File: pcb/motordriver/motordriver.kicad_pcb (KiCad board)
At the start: 2 copper layers, 15 parts, among them J1 Conn_01x03_Pin, J2 Conn_01x02_Pin, J3 Conn_01x02_Pin, J4 Conn_01x03_Pin, U1 ESP32-CAM, U2 DRV8833PWP

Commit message: PCB created
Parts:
- removed U1: ESP32-CAM, _for_motordriver:ESP32-CAM
- added C5: 22uF, Capacitor_SMD:C_1206_3216Metric, F.Cu at (103.5, 120.4)
- added C6: 22uF, Capacitor_SMD:C_1206_3216Metric, F.Cu at (145.1, 119.8)
- added H1: ~, PCM_JLCPCB:Hole_Tooling_JLCPCB, F.Cu at (101.5, 101.5)
- added H2: ~, PCM_JLCPCB:Hole_Tooling_JLCPCB, F.Cu at (101.5, 123.5)
- added H3: ~, PCM_JLCPCB:Hole_Tooling_JLCPCB, F.Cu at (147.5, 101.5)
- added J5: Conn_02x03_Odd_Even, Connector_PinHeader_2.54mm:PinHeader_2x03_P2.54mm_Horizontal, F.Cu at (141.6, 116.6)
- added R6: 5k1, Resistor_SMD:R_0603_1608Metric, F.Cu at (116.0, 104.2)
- added R7: 5k1, Resistor_SMD:R_0603_1608Metric, F.Cu at (117.8, 103.5)
- C3: renamed from C2; value 10uF -> 22uF; footprint Capacitor_SMD:C_1210_3225Metric -> Capacitor_SMD:C_1206_3216Metric
- C4: value 10uF -> 22uF; footprint Capacitor_SMD:C_1210_3225Metric -> Capacitor_SMD:C_1206_3216Metric
- J1: value Conn_01x03_Pin -> USB_C_Receptacle_PowerOnly_6P; footprint Connector_PinHeader_2.54mm:PinHeader_1x03_P2.54mm_Horizontal -> Connector_USB:USB_C_Receptacle_HRO_TYPE-C-31-M-17
- J2, J3: value Conn_01x02_Pin -> Conn_01x08_Pin; footprint Connector_PinHeader_2.54mm:PinHeader_1x02_P2.54mm_Vertical -> Connector_PinSocket_2.54mm:PinSocket_1x08_P2.54mm_Vertical
- J4: value Conn_01x03_Pin -> Conn_02x03_Odd_Even; footprint Connector_PinHeader_2.54mm:PinHeader_1x03_P2.54mm_Horizontal -> Connector_PinHeader_2.54mm:PinHeader_2x03_P2.54mm_Horizontal
- moved U2 62.2 mm to (124.1, 116.0)
- moved J2 60.8 mm to (136.0, 119.8), turned to 180 degrees
- moved C4 56.0 mm to (131.6, 120.4)
- moved R5 55.7 mm to (108.3, 120.4)
- moved R4 54.9 mm to (140.2, 119.8)
- moved R3 54.0 mm to (116.3, 118.4), turned to 90 degrees
- moved R1 53.7 mm to (120.0, 110.5), turned to 180 degrees
- moved C1 52.8 mm to (129.4, 113.6), turned to -90 degrees
- moved C3 52.5 mm to (124.9, 110.5)
- moved C2 52.5 mm to (129.2, 116.9), turned to -90 degrees
- moved R2 52.5 mm to (116.3, 113.6), turned to -90 degrees
- moved J4 49.6 mm to (102.5, 116.6), turned to 90 degrees
- moved J3 47.7 mm to (113.0, 102.0)
- moved J1 45.5 mm to (124.5, 104.0), turned to 180 degrees
- renumbered C3 to C2
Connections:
- J2 pad 1: Net-(J2-Pin_1) -> +5V
- J2 pad 2: Net-(J2-Pin_2) -> GND
- J3 pad 1: Net-(J3-Pin_1) -> GND
- J3 pad 2: Net-(J3-Pin_2) -> unconnected-(J3-Pin_2-Pad2)
- J4 pad 1: GND -> unconnected-(J4-Pin_1-Pad1)
- J4 pad 2: Net-(J4-Pin_2) -> /Servo2
- J4 pad 3: /Servo2 -> Net-(J4-Pin_3)
- R4 pad 2: Net-(J1-Pin_2) -> Net-(J5-Pin_4)
- R5 pad 1: +5V -> Net-(J4-Pin_4)
- R5 pad 2: Net-(J4-Pin_2) -> +5V
- U2 pad 2: Net-(J2-Pin_2) -> Net-(J4-Pin_3)
- U2 pad 4: Net-(J2-Pin_1) -> Net-(J4-Pin_5)
- U2 pad 5: Net-(J3-Pin_1) -> Net-(J5-Pin_5)
- U2 pad 7: Net-(J3-Pin_2) -> Net-(J5-Pin_3)
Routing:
- net +5V: track 0.00 -> 59.5 mm, vias 0 -> 4
- net Net-(J5-Pin_5): track 0.00 -> 43.2 mm, vias 0 -> 2
- net Net-(J5-Pin_3): track 0.00 -> 35.5 mm
- net Net-(U2-VM): track 0.00 -> 22.7 mm, vias 0 -> 2
- net /MotorL2: track 0.00 -> 20.6 mm
- net GND: track 0.00 -> 20.6 mm, vias 0 -> 16
- net /MotorL1: track 0.00 -> 19.0 mm, vias 0 -> 1
- net Net-(J4-Pin_3): track 0.00 -> 17.9 mm
- net Net-(J4-Pin_5): track 0.00 -> 14.1 mm
- net /Servo2: track 0.00 -> 13.5 mm
- net /Servo1: track 0.00 -> 12.6 mm
- net /MotorR1: track 0.00 -> 11.9 mm, vias 0 -> 2
- net /MotorR2: track 0.00 -> 10.1 mm
- net Net-(J1-CC2): track 0.00 -> 9.53 mm
- net Net-(J4-Pin_4): track 0.00 -> 9.22 mm
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- added copper zone on B.Cu, net +5V
- added copper zone on B.Cu, net GND
- added copper zone on F.Cu, net GND
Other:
- board outline added: 49 x 25 mm
- board text added: "JLCJLCJLCJLC"
- board text added: "Motor driver for ESP-CAM, LL2026 Hackerspace FFM e.V. https://github.com/hackffm/ESP32_CAM_Auto"
- board text added: "MotorLeft Servo1"
- board text added: "MotorRight Servo2"

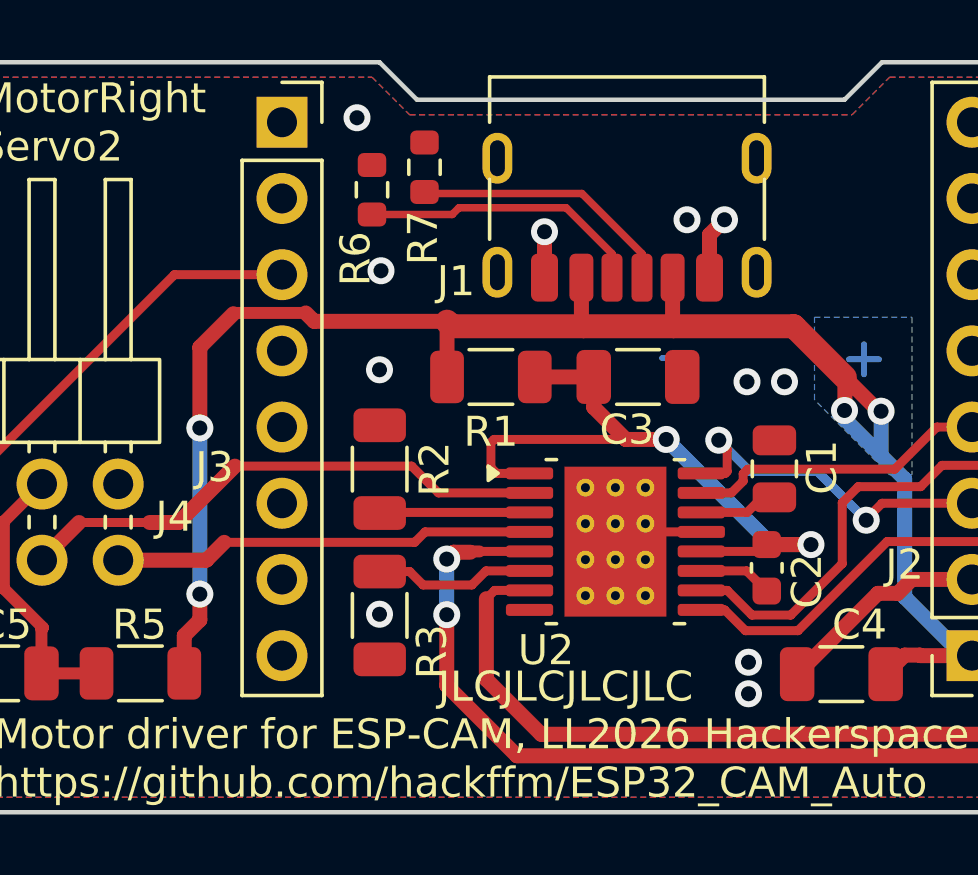
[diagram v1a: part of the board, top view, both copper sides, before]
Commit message: Updated PCB, fixed minor bugs on PCB
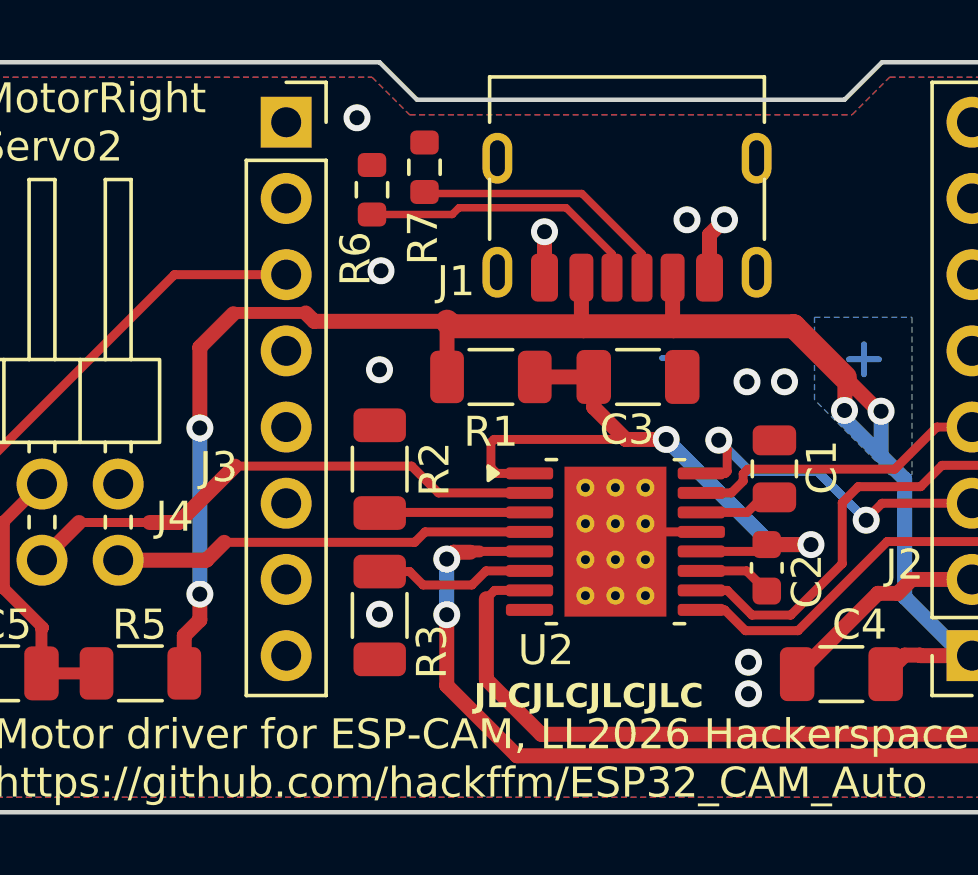
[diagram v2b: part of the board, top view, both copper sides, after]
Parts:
- added PN1: ~, PCM_JLCPCB:Part_Num_JLCPCB, F.Cu at (123.2, 121.1)
- moved J3 0.14 mm to (113.1, 102.0)
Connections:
- J3 pad 1: GND -> unconnected-(J3-Pin_1-Pad1)
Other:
- board text removed: "JLCJLCJLCJLC"
